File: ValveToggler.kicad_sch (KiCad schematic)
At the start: 68 parts, among them J1 24V IN, J17 MODE (24V), J2 Coil2, J3 Coil1, Q1 IRFZ24N, Q11 2N7000, Q2 2N7000, Q3 IRFZ24N, Q4 2N7000, Q7 2N7000, Q9 2N7000, U2 NE555P, U3 L7812, U4 NE555P, U9 LM2576T-5

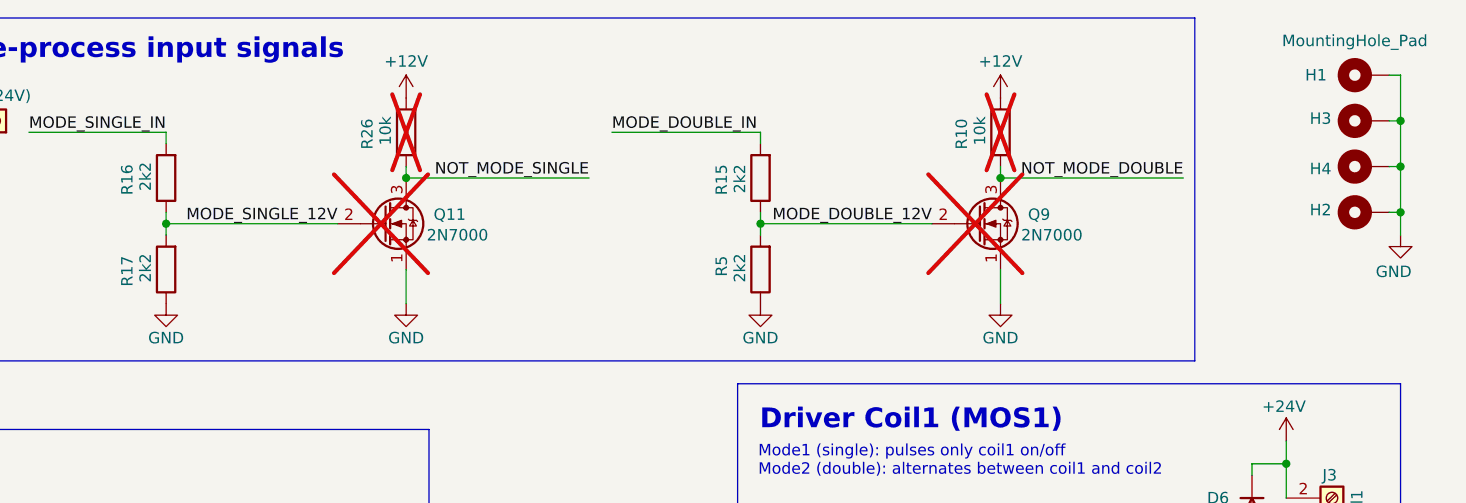
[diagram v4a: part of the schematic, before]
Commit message: Final adjustments pre milling: Mounthole, Text layer, Text thickness
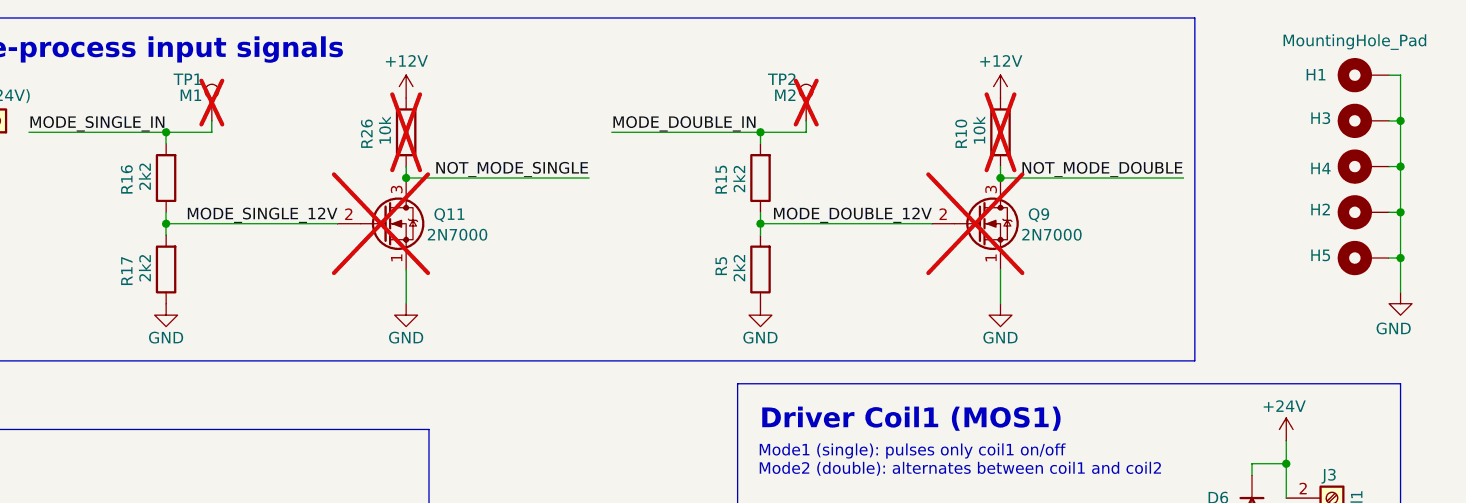
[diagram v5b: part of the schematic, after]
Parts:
- added H5: MountingHole_Pad, mountingHoles_libJonny:MountingHole_2.2mm_NPTH-with-pad_DRC-clearance-error, symbol Mechanical:MountingHole_Pad
- added TP1: M1, Connector_PinHeader_2.54mm:PinHeader_1x01_P2.54mm_Vertical, symbol Connector:TestPoint
- added TP2: M2, Connector_PinHeader_2.54mm:PinHeader_1x01_P2.54mm_Vertical, symbol Connector:TestPoint
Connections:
- net GND: now also H5.1
- net MODE_DOUBLE_IN: now also TP2.1
- net MODE_SINGLE_IN: now also TP1.1

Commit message: Arrange Fab text, Update actually soldered Values, Add milled gerber export
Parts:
- removed D1: TVS 5V, Diode_THT:D_5W_P5.08mm_Vertical_AnodeUp, symbol Diode:PTVS5V0Z1USK
- removed OC21: LTV-817, Package_DIP:DIP-4_W10.16mm_LongPads, symbol Optocoupler_AKL:LTV-817
- removed Q2: 2N7000, Package_TO_SOT_THT:TO-92_HandSolder, symbol Transistor_FET:2N7000
- removed R2: 200, Resistor_THT:R_Axial_DIN0207_L6.3mm_D2.5mm_P2.54mm_Vertical, symbol Device:R
- removed R3: 2k2, Resistor_THT:R_Axial_DIN0207_L6.3mm_D2.5mm_P2.54mm_Vertical, symbol Device:R
- removed R76: 330, Resistor_THT:R_Axial_DIN0207_L6.3mm_D2.5mm_P2.54mm_Vertical, symbol Device:R
- removed R77: 4k7, Resistor_THT:R_Axial_DIN0207_L6.3mm_D2.5mm_P10.16mm_Horizontal, symbol Device:R
- removed TP12: TP-servoPWM, Connector_PinHeader_2.54mm:PinHeader_1x01_P2.54mm_Vertical, symbol Connector:TestPoint
- R13: value 1k5_t-onMin -> 2k2_t-onMin
- RV1: value 50k_freq1 -> 100k_freq1
- RV3: value 50k_t-on -> 10k_t-on
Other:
- note added: "OFF: 3k3...103.3k -> 100ms...3.36s ON: 2k2...12.2k -> 72ms...400s"
- note removed: "Isolated PWM Signal out (Servo)"
- note removed: "OFF: 3k3...103.3k -> 100ms...3.36s ON: 1k5...101.5k -> 49ms...3.3s"
- moved on the sheet: C1, C2, R1, RV1, U2

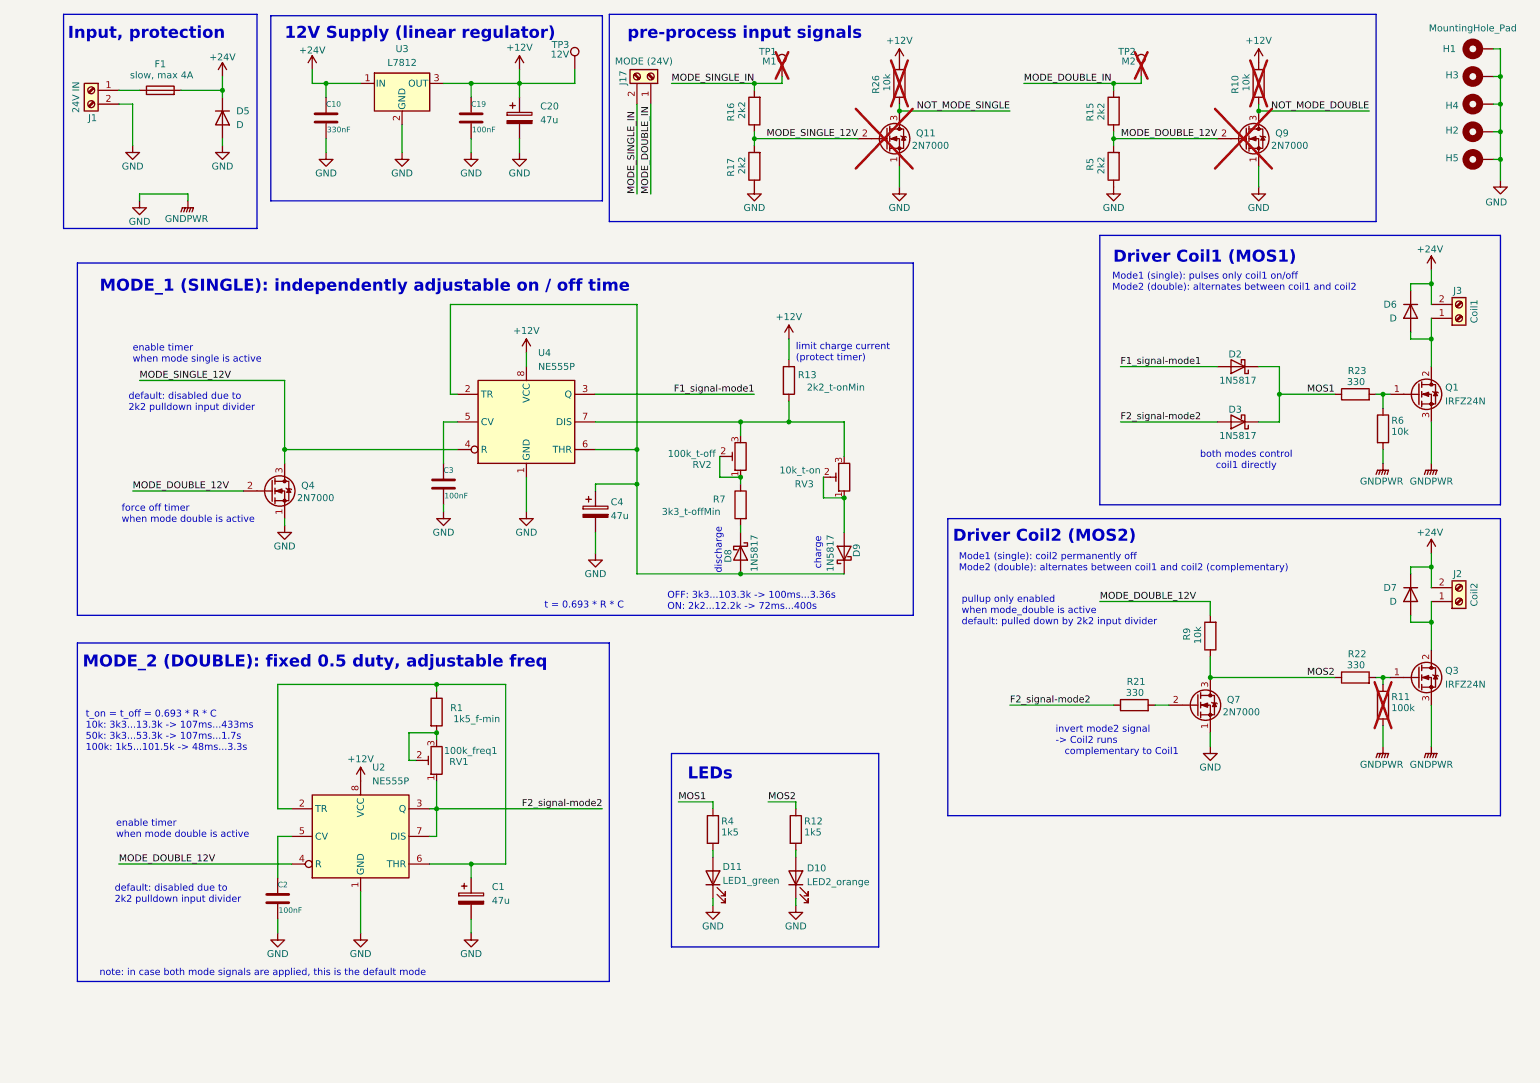
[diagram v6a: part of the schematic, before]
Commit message: Fix mos1 not turning fully on (rework leds), Fix swapped text, Add changelog
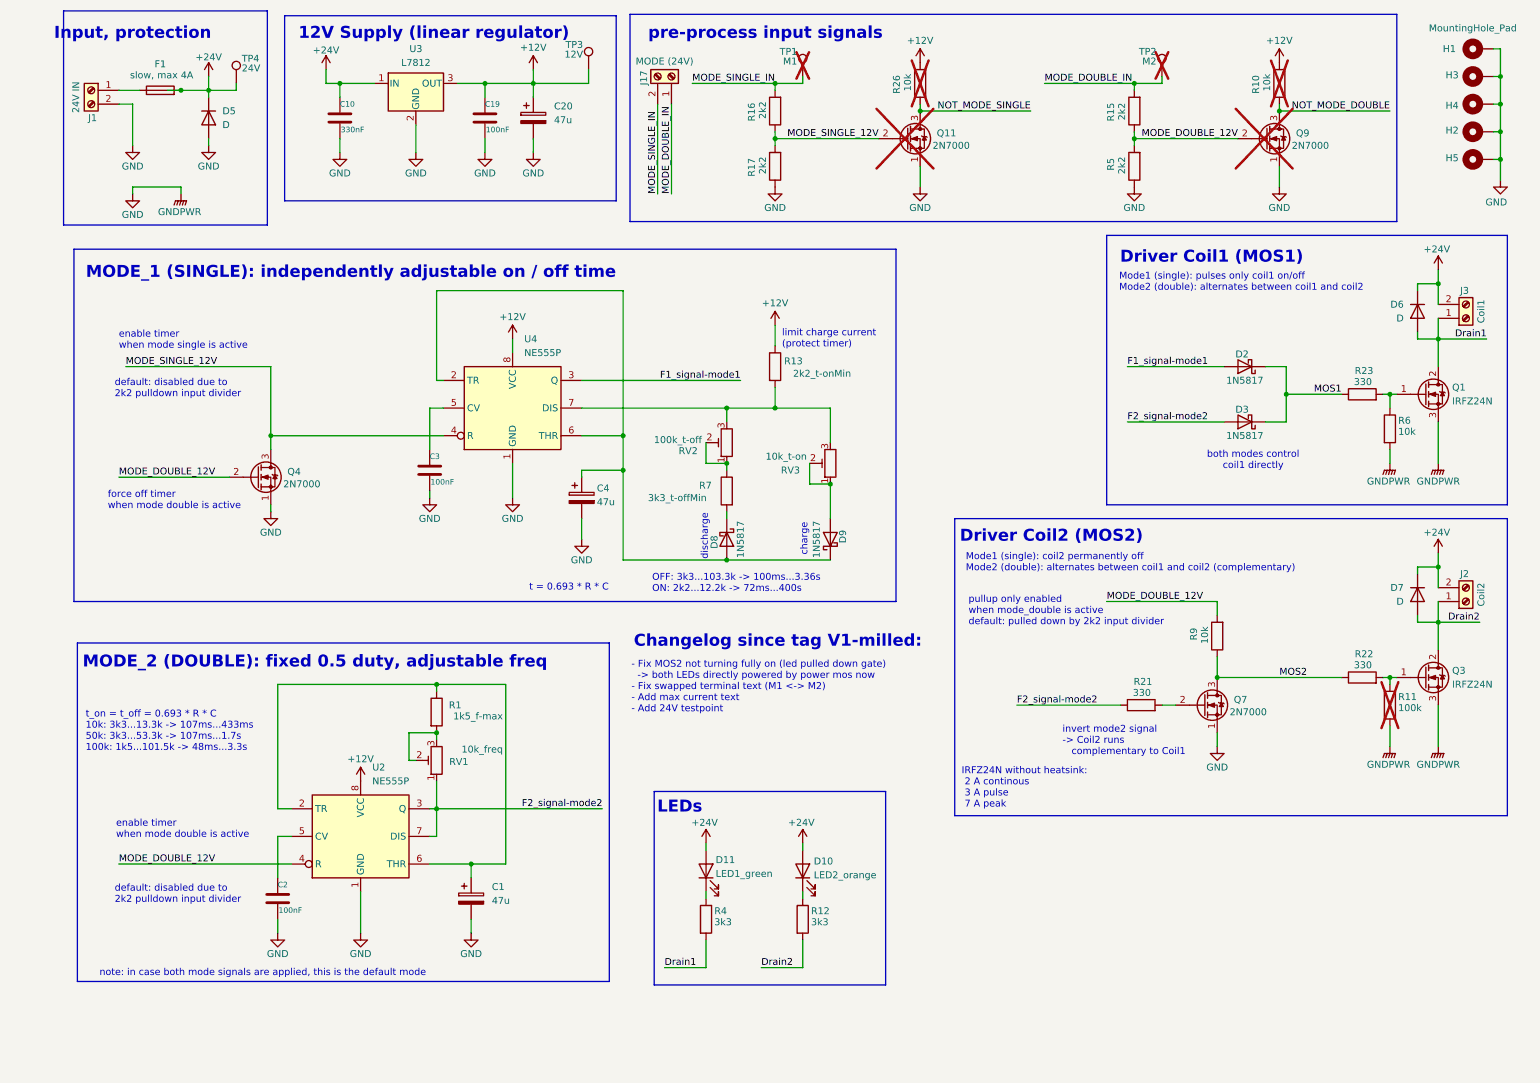
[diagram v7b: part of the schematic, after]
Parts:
- added TP4: 24V, Connector_PinHeader_2.54mm:PinHeader_1x01_P2.54mm_Vertical, symbol Connector:TestPoint
- R1: value 1k5_f-min -> 1k5_f-max
- R12, R4: value 1k5 -> 3k3
- RV1: value 100k_freq1 -> 10k_freq
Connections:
- net +24V: now also D10.2 (A), D11.2 (A), TP4.1
- net GND: no longer D10.1 (K), D11.1 (K)
- net MOS1: no longer R4.1
- net MOS2: no longer R12.1
- net Drain2: now reaches D7.2 (A), J2.1 (Pin_1), Q3.2 (D)
- net Drain2: now also R12.2
- net Drain1: now reaches D6.2 (A), J3.1 (Pin_1), Q1.2 (D)
- net Drain1: now also R4.2
- new net: D11.1 (K), R4.1
- new net: D10.1 (K), R12.1
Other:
- note added: "- Fix MOS2 not turning fully on (led pulled down gate) -> both LEDs directly powered by power mos now - Fix swapped terminal text (M1 <-> M2) - Add max current text - Add 24V testpoint"
- note added: "Changelog since tag V1-milled:"
- note added: "IRFZ24N without heatsink: 2 A continous 3 A pulse 7 A peak"
- moved on the sheet: C10, C19, C20, C3, C4, D10, D11, D2, D3, D5, D6, D7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
